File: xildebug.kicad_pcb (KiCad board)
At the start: 2 copper layers, 42 x 46.2 mm, 64 parts, among them J1 USB_B_Micro, J2 Conn_STM_SWD, J3 Conn_Ext1, J4 Conn_Ext2, J5 Conn_DUT, J6 Conn_DUT_VDD, U1 XC6206P332MR, U2 MAX14662, U3 STM32L433CCUx, U4 TS5A3167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

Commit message: Add DUT silk
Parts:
- moved D5 9.01 mm to (208.4, 57.7)
- moved D6 9.01 mm to (204.2, 57.7)
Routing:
- net /DUT_SWCLK_B: track 25.6 -> 7.24 mm, vias 0 -> 1
- net /DUT_SWDIO_B: track 19.3 -> 6.21 mm, vias 0 -> 1
- net Net-(D6-Pad1): track 5.59 -> 14.9 mm
- net Net-(D5-Pad2): track 4.74 -> 13.9 mm
- net /DUT_UART_RX_B: track 19.0 -> 27.9 mm
- net /DUT_UART_TX_B: track 7.78 -> 16.3 mm
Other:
- board text added: "3V"
- board text added: "CLK"
- board text added: "IO"
- board text added: "Vdut"
- board text removed: "VDD CLK GND IO TX RX"
- board text removed: "Vout"

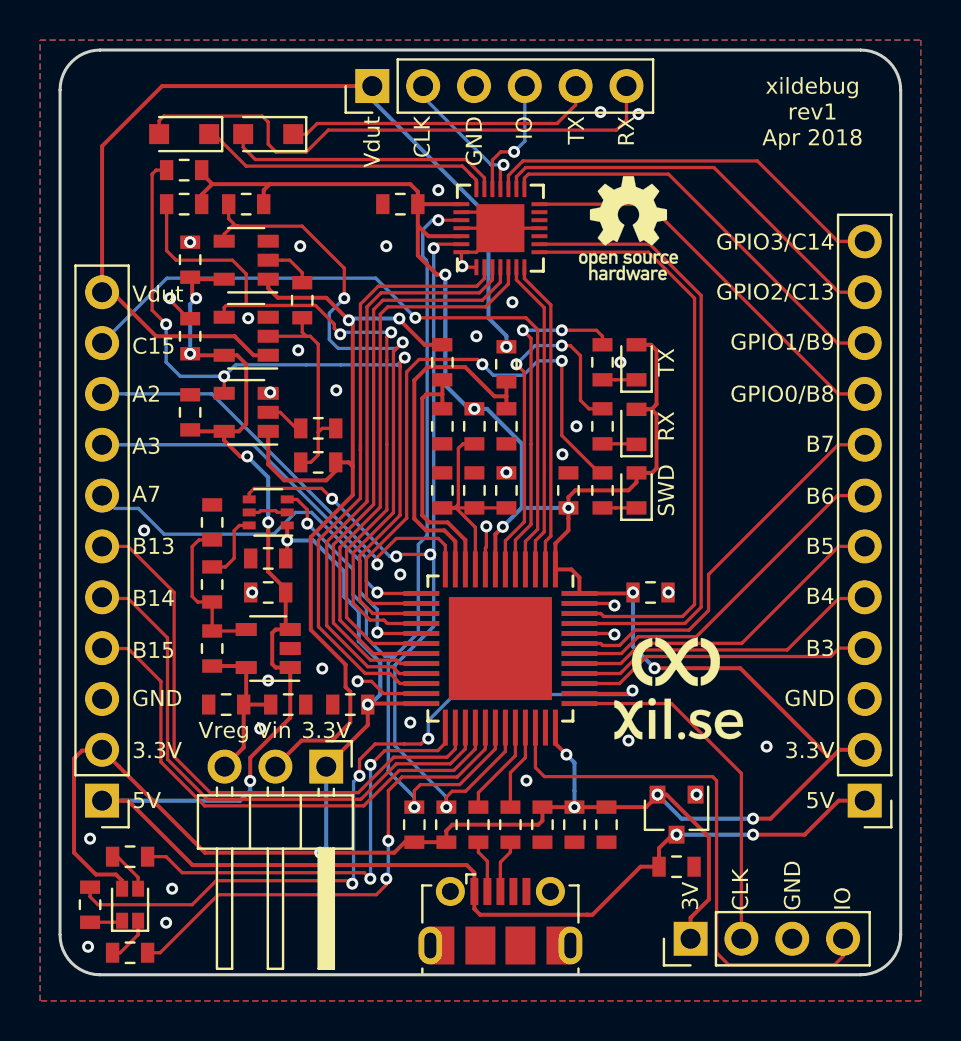
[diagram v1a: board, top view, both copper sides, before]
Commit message: Add button on BOOT0
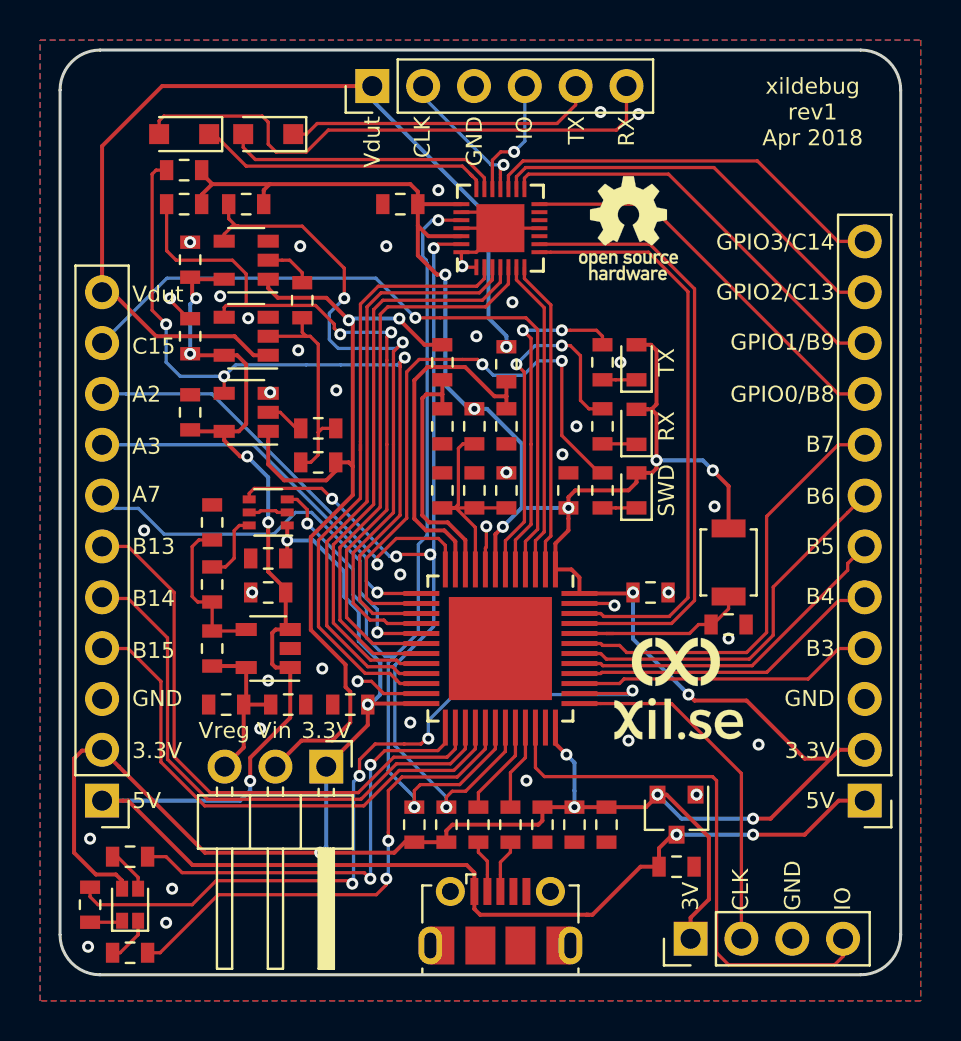
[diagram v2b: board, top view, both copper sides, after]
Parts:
- added R23: 10K, Resistor_SMD:R_0603_1608Metric, F.Cu at (231.4, 82.2)
- added SW1: BOOT0, Button_Switch_SMD:SW_SPST_B3U-1000P, F.Cu at (231.4, 79.1)
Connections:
- U3 pad 44: GND -> Net-(R23-Pad1)
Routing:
- net Net-(R23-Pad1): track 0.00 -> 8.93 mm
- net +3V3: track 170.9 -> 176.9 mm, vias 13 -> 15
- net /PB7: track 19.5 -> 22.1 mm
- net GND: track 22.7 -> 20.9 mm, vias 38 -> 40
- net /PB6: track 17.5 -> 19.2 mm
- net /GPIO1_A: track 30.1 -> 29.4 mm
- net /GPIO0_A: track 31.1 -> 30.5 mm
